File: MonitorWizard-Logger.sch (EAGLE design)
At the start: 38 parts, among them CON1 MICROSD, IC1 LD117AV33, J1 22-27-2041-04, J2 22-27-2041-04, J3 22-27-2041-04, U1 DHT22, U2 RFM69HW, U3 LTC3531, U4-NRF24L01 NRF24L01+-PCB-AERIAL, U6 ATMEGA328P-PU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

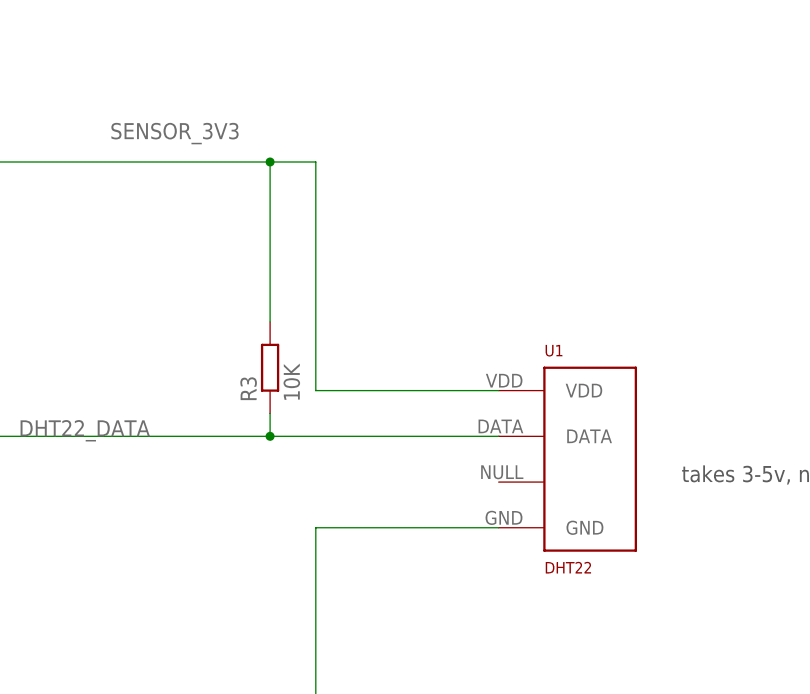
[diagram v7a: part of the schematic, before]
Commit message: Move some stuff around, add a filter capacitor. As ordered from Screenbond
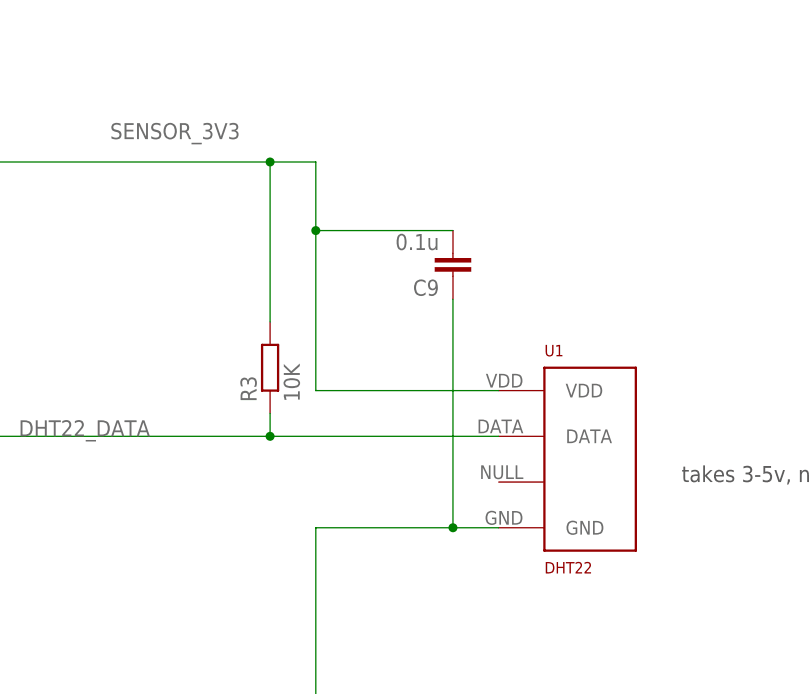
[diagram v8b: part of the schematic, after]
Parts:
- added C9: 0.1u, rcl:C-EU025-024X044
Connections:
- net GND: now also C9.1
- net SENSOR_3V3: now also C9.2
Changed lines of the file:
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@@
 <part name="JP2" library="SparkFun-Connectors" deviceset="POWER_JACK" device="PTH"/>
 <part name="U3" library="custom" deviceset="LTC3531" device=""/>
+<part name="C9" library="rcl" deviceset="C-EU" device="025-024X044" value="0.1u"/>
 </parts>
 <sheets>
@@
 <instance part="JP2" gate="G$1" x="307.34" y="-360.68"/>
 <instance part="U3" gate="G$1" x="584.2" y="-312.42"/>
+<instance part="C9" gate="G$1" x="139.7" y="-345.44" rot="R180"/>
 </instances>
 <busses>
@@
 <wire x1="-12.7" y1="-411.48" x2="-15.24" y2="-411.48" width="0.1524" layer="91"/>
 <wire x1="-15.24" y1="-411.48" x2="-25.4" y2="-411.48" width="0.1524" layer="91"/>
-<wire x1="144.78" y1="-373.38" x2="124.46" y2="-373.38" width="0.1524" layer="91"/>
+<wire x1="144.78" y1="-373.38" x2="139.7" y2="-373.38" width="0.1524" layer="91"/>
+<wire x1="139.7" y1="-373.38" x2="124.46" y2="-373.38" width="0.1524" layer="91"/>
 <wire x1="124.46" y1="-373.38" x2="124.46" y2="-411.48" width="0.1524" layer="91"/>
 <junction x="124.46" y="-411.48"/>
@@
 <wire x1="-15.24" y1="-350.52" x2="-15.24" y2="-411.48" width="0.1524" layer="91"/>
 <junction x="-15.24" y="-411.48"/>
+<pinref part="C9" gate="G$1" pin="1"/>
+<wire x1="139.7" y1="-347.98" x2="139.7" y2="-373.38" width="0.1524" layer="91"/>
+<junction x="139.7" y="-373.38"/>
 </segment>
 </net>
@@
 <pinref part="U1" gate="G$1" pin="VDD"/>
 <wire x1="144.78" y1="-358.14" x2="124.46" y2="-358.14" width="0.1524" layer="91"/>
-<wire x1="124.46" y1="-358.14" x2="124.46" y2="-332.74" width="0.1524" layer="91"/>
+<wire x1="124.46" y1="-358.14" x2="124.46" y2="-340.36" width="0.1524" layer="91"/>
 <pinref part="R3" gate="G$1" pin="2"/>
+<wire x1="124.46" y1="-340.36" x2="124.46" y2="-332.74" width="0.1524" layer="91"/>
 <wire x1="119.38" y1="-350.52" x2="119.38" y2="-332.74" width="0.1524" layer="91"/>
 <label x="101.6" y="-330.2" size="1.778" layer="95"/>
@@
 <wire x1="119.38" y1="-332.74" x2="-30.48" y2="-332.74" width="0.1524" layer="91"/>
 <junction x="-30.48" y="-332.74"/>
-</segment>
-</net>
+<pinref part="C9" gate="G$1" pin="2"/>
+<wire x1="124.46" y1="-340.36" x2="139.7" y2="-340.36" width="0.1524" layer="91"/>
+<junction x="124.46" y="-340.36"/>
+</segment>
+</net>
